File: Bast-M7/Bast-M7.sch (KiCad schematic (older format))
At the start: 88 parts, among them J1 Conn_Battery, J2 SWD, J3 Conn_Left, J4 Conn_Right, P1 USB_C_Plug_USB2.0, Q1 TP0610L, SW1 RESET, SW2 ONOFF, SW3 SW_DIP_x04, U1 W25Q128JVS, U2 MIMXRT1011DAE5A, U3 MCP73831-3-OT, U4 AP63203WU-7, Y1 24Mhz, Y2 32.768KHZ

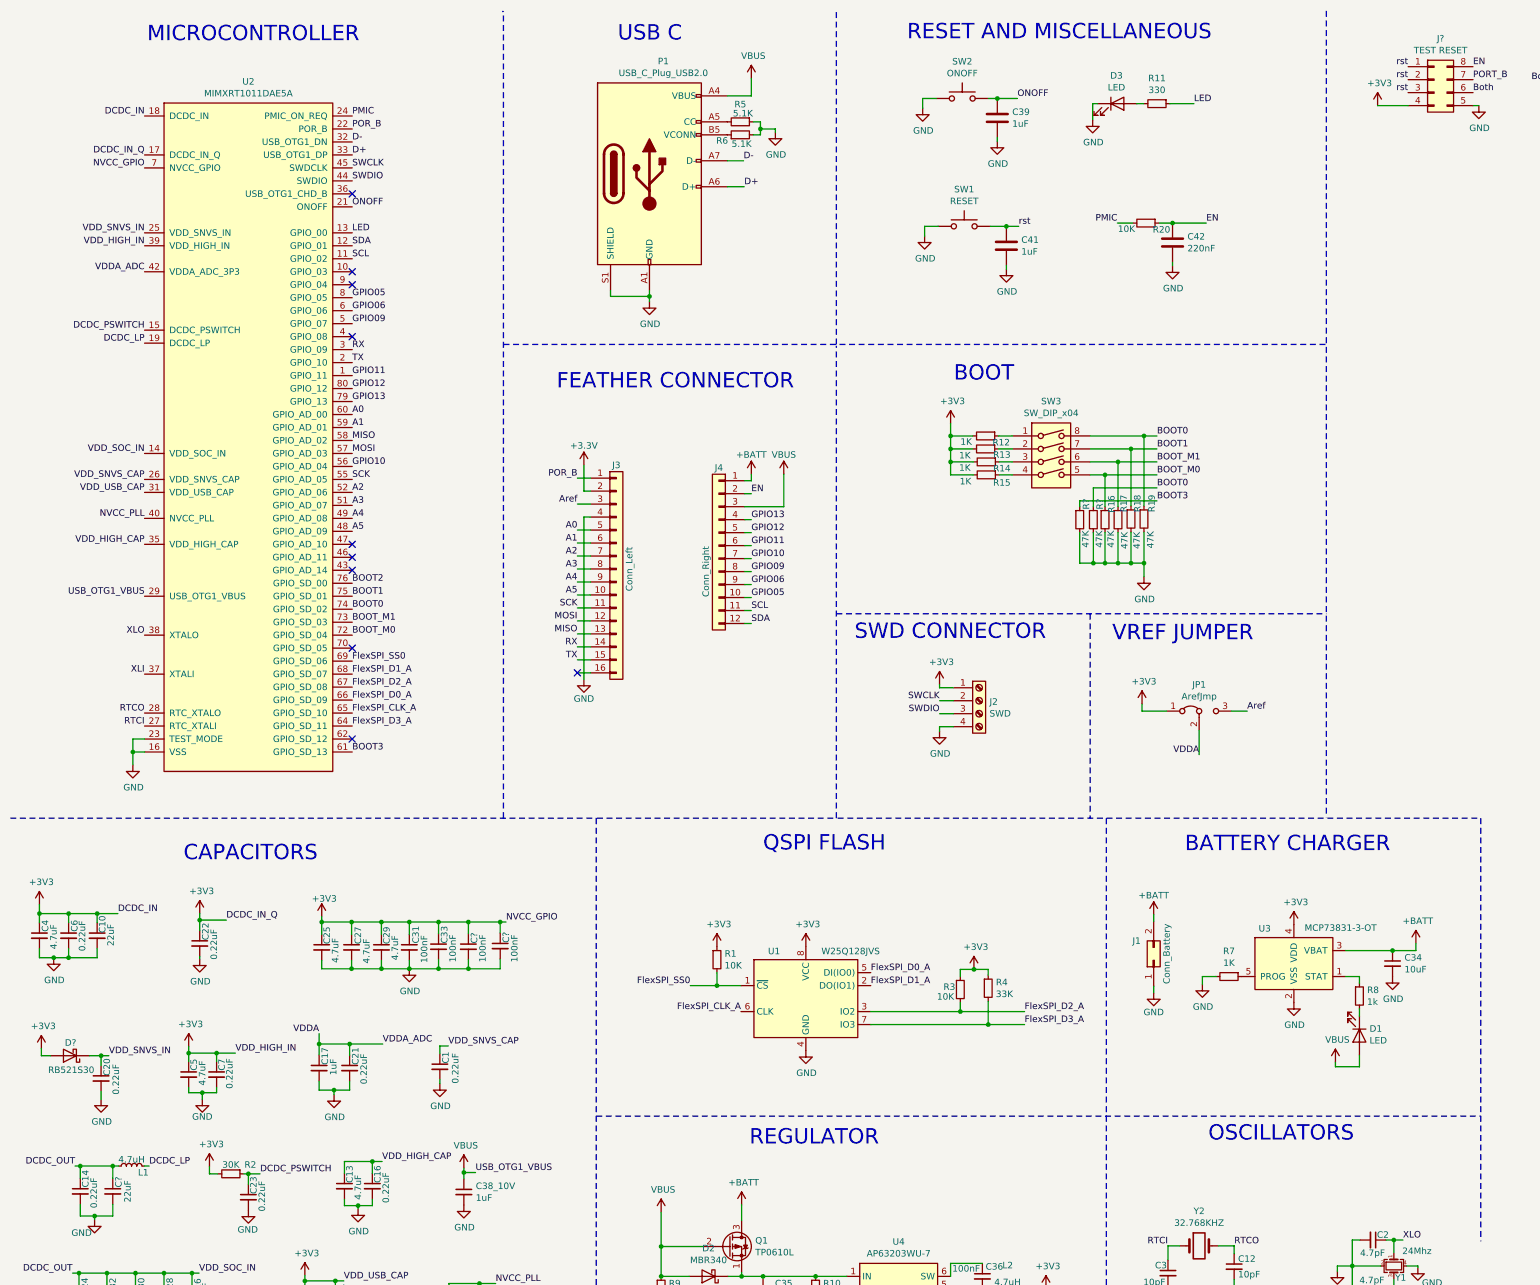
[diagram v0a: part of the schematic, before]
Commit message: boot label fixed
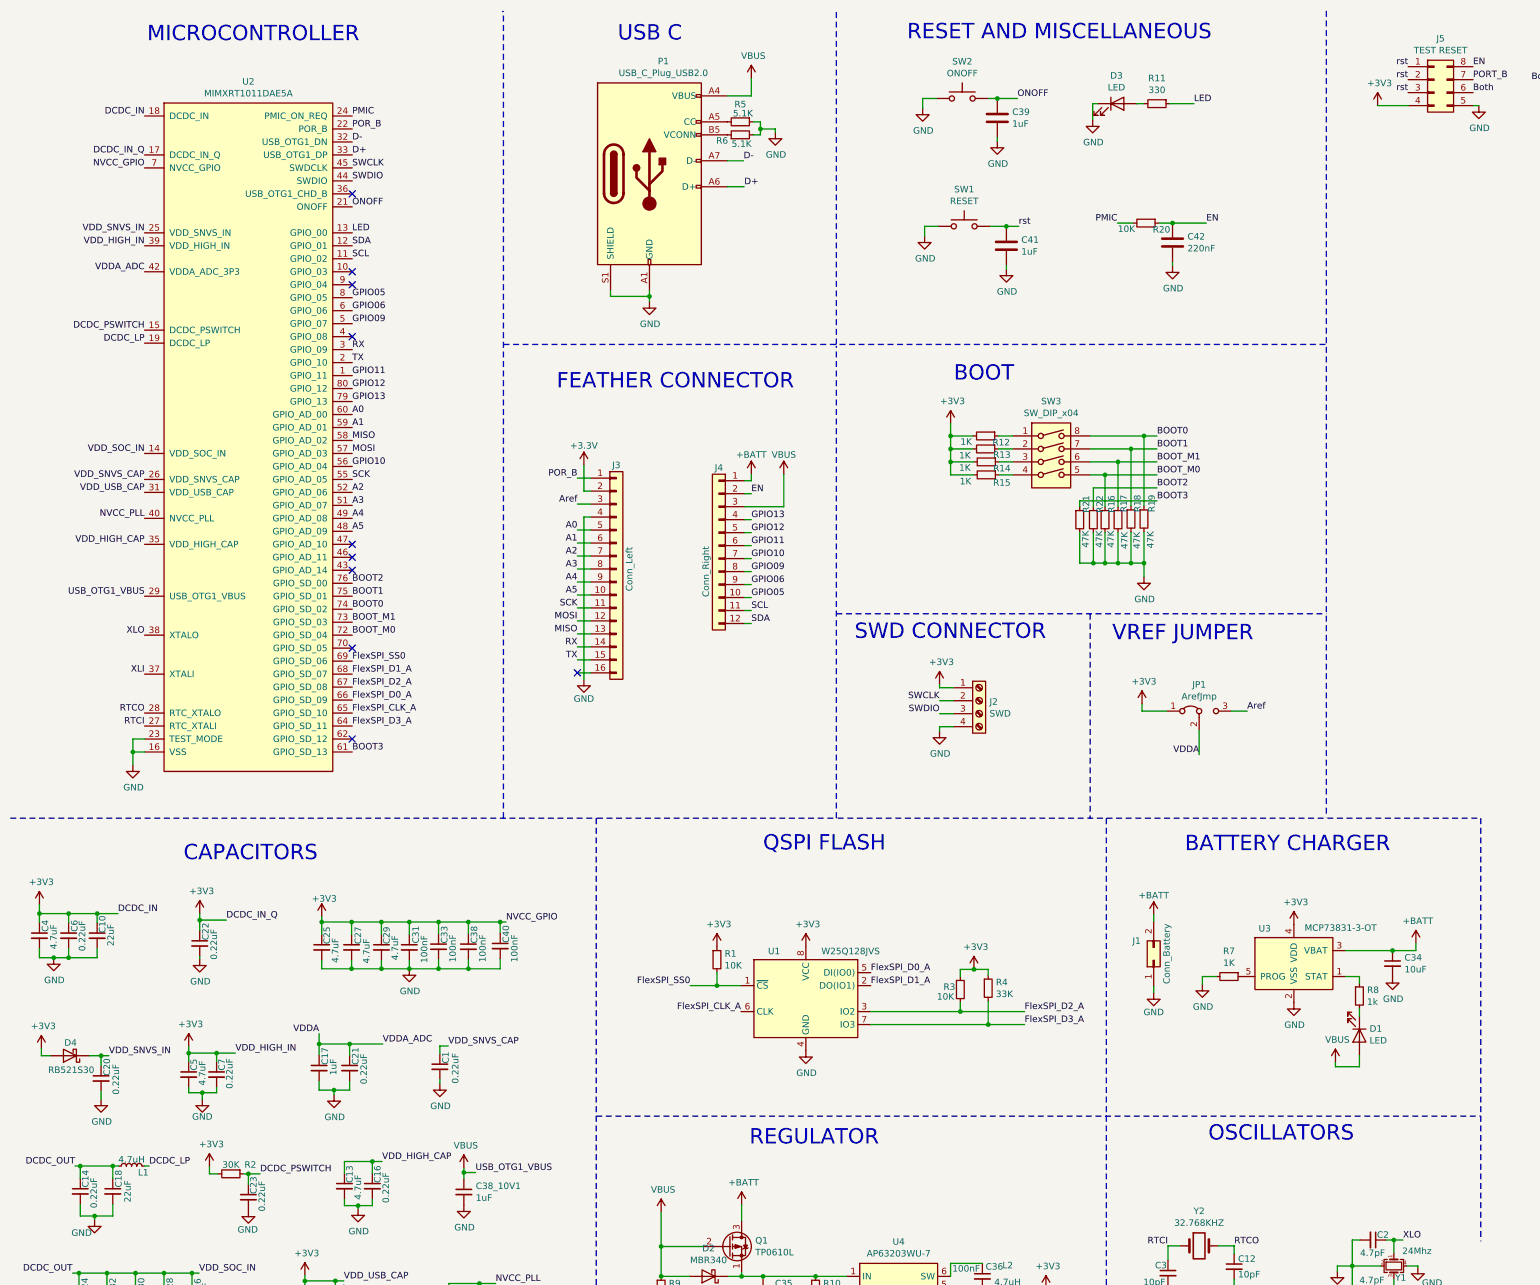
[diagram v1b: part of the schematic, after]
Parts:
- gave numbers to parts that had none: 7
- renumbered C38_10V to C38_10V1
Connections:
- net BOOT0: no longer R22.1
- net BOOT2: now also R22.1
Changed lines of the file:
@@
 NoConn ~ 3115 1890
 $Comp
-L Device:C_Small C38_10V
+L Device:C_Small C38_10V1
 U 1 1 5EC24D8C
 P 3975 9580
-F 0 "C38_10V" H 4067 9626 50  0000 L CNN
+F 0 "C38_10V1" H 4067 9626 50  0000 L CNN
 F 1 "1uF" H 4067 9535 50  0000 L CNN
 F 2 "" H 3975 9580 50  0001 C CNN
@@
 BOOT_M1
 Text Label 9315 4155 0    50   ~ 0
-BOOT0
+BOOT2
 Text Label 9315 4255 0    50   ~ 0
 BOOT3
@@
 	9015 3955 9315 3955
 $Comp
-L Device:R_Small R?
+L Device:R_Small R22
 U 1 1 5F297FC1
 P 8825 4400
-F 0 "R?" V 8875 4520 50  0000 C CNN
+F 0 "R22" V 8875 4520 50  0000 C CNN
 F 1 "47K" V 8870 4250 50  0000 C CNN
 F 2 "" H 8825 4400 50  0001 C CNN
@@
 $EndComp
 $Comp
-L Device:R_Small R?
+L Device:R_Small R21
 U 1 1 5F2AEC5F
 P 8720 4400
-F 0 "R?" V 8770 4520 50  0000 C CNN
+F 0 "R21" V 8770 4520 50  0000 C CNN
 F 1 "47K" V 8765 4250 50  0000 C CNN
 F 2 "" H 8720 4400 50  0001 C CNN
@@
 	8825 4735 8915 4735
 $Comp
-L power:+3V3 #PWR?
+L power:+3V3 #PWR08
 U 1 1 5F41D099
 P 2750 10225
-F 0 "#PWR?" H 2750 10075 50  0001 C CNN
+F 0 "#PWR08" H 2750 10075 50  0001 C CNN
 F 1 "+3V3" H 2765 10398 50  0000 C CNN
 F 2 "" H 2750 10225 50  0001 C CNN
@@
 Connection ~ 705  7435
 $Comp
-L Device:D_Schottky D?
+L Device:D_Schottky D4
 U 1 1 5F7C0D4D
 P 940 8530
-F 0 "D?" H 935 8430 50  0000 C CNN
+F 0 "D4" H 935 8430 50  0000 C CNN
 F 1 "RB521S30" H 930 8640 50  0000 C CNN
 F 2 "" H 940 8530 50  0001 C CNN
@@
 $EndComp
 $Comp
-L power:+3V3 #PWR?
+L power:+3V3 #PWR05
 U 1 1 5F7C24FB
 P 720 8475
-F 0 "#PWR?" H 720 8325 50  0001 C CNN
+F 0 "#PWR05" H 720 8325 50  0001 C CNN
 F 1 "+3V3" H 735 8648 50  0000 C CNN
 F 2 "" H 720 8475 50  0001 C CNN
@@
 	1855 8510 2070 8510
 $Comp
-L power:+3V3 #PWR?
+L power:+3V3 #PWR07
 U 1 1 5F9F4723
 P 1855 8460
-F 0 "#PWR?" H 1855 8310 50  0001 C CNN
+F 0 "#PWR07" H 1855 8310 50  0001 C CNN
 F 1 "+3V3" H 1870 8633 50  0000 C CNN
 F 2 "" H 1855 8460 50  0001 C CNN
@@
 	1855 8510 1855 8575
 $Comp
-L Device:C_Small C?
+L Device:C_Small C38
 U 1 1 5FCD5A95
 P 4010 7690
-F 0 "C?" V 4055 7715 50  0000 L CNN
+F 0 "C38" V 4055 7715 50  0000 L CNN
 F 1 "100nF" V 4120 7570 50  0000 L CNN
 F 2 "" H 4010 7690 50  0001 C CNN
@@
 $EndComp
 $Comp
-L Device:C_Small C?
+L Device:C_Small C40
 U 1 1 5FCD5DD6
 P 4255 7685
-F 0 "C?" V 4300 7710 50  0000 L CNN
+F 0 "C40" V 4300 7710 50  0000 L CNN
 F 1 "100nF" V 4365 7560 50  0000 L CNN
 F 2 "" H 4255 7685 50  0001 C CNN
@@
 Connection ~ 4255 7500
 $Comp
-L power:GND #PWR?
+L power:GND #PWR09
 U 1 1 5FF842BF
 P 3555 7860
-F 0 "#PWR?" H 3555 7610 50  0001 C CNN
+F 0 "#PWR09" H 3555 7610 50  0001 C CNN
 F 1 "GND" H 3560 7687 50  0000 C CNN
 F 2 "" H 3555 7860 50  0001 C CNN
@@
 DCDC_LP
 $Comp
-L Device:C_Small C?
+L Device:C_Small C18
 U 1 1 602BE064
 P 1270 9575
-F 0 "C?" V 1315 9605 50  0000 L CNN
+F 0 "C18" V 1315 9605 50  0000 L CNN
 F 1 "22uF" V 1385 9490 50  0000 L CNN
 F 2 "" H 1270 9575 50  0001 C CNN
@@
 	1550 9380 1515 9380
 $Comp
-L power:GND #PWR?
+L power:GND #PWR06
 U 1 1 605F7E32
 P 1445 10590
-F 0 "#PWR?" H 1445 10340 50  0001 C CNN
+F 0 "#PWR06" H 1445 10340 50  0001 C CNN
 F 1 "GND" H 1345 10490 50  0000 C CNN
 F 2 "" H 1445 10590 50  0001 C CNN
@@
 Connection ~ 11140 9950
 $Comp
-L power:GND #PWR?
+L power:GND #PWR011
 U 1 1 60D25C57
 P 11325 10160
-F 0 "#PWR?" H 11325 9910 50  0001 C CNN
+F 0 "#PWR011" H 11325 9910 50  0001 C CNN
 F 1 "GND" H 11435 10040 50  0000 C CNN
 F 2 "" H 11325 10160 50  0001 C CNN
@@
 Connection ~ 12415 1025
 $Comp
-L Connector_Generic:Conn_02x04_Counter_Clockwise J?
+L Connector_Generic:Conn_02x04_Counter_Clockwise J5
 U 1 1 61C811B9
 P 11450 1010
-F 0 "J?" H 11500 1327 50  0000 C CNN
+F 0 "J5" H 11500 1327 50  0000 C CNN
 F 1 "TEST RESET" H 11500 1236 50  0000 C CNN
 F 2 "" H 11450 1010 50  0001 C CNN
@@
 $EndComp
 $Comp
-L power:+3V3 #PWR?
+L power:+3V3 #PWR010
 U 1 1 61C81B5D
 P 11015 1210
-F 0 "#PWR?" H 11015 1060 50  0001 C CNN
+F 0 "#PWR010" H 11015 1060 50  0001 C CNN
 F 1 "+3V3" H 11030 1383 50  0000 C CNN
 F 2 "" H 11015 1210 50  0001 C CNN
@@
 	11250 1210 11015 1210
 $Comp
-L power:GND #PWR?
+L power:GND #PWR012
 U 1 1 61D0690C
 P 11795 1210
-F 0 "#PWR?" H 11795 960 50  0001 C CNN
+F 0 "#PWR012" H 11795 960 50  0001 C CNN
 F 1 "GND" H 11800 1037 50  0000 C CNN
 F 2 "" H 11795 1210 50  0001 C CNN
